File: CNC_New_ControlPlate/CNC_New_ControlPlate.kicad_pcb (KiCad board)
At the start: 2 copper layers, 1 part

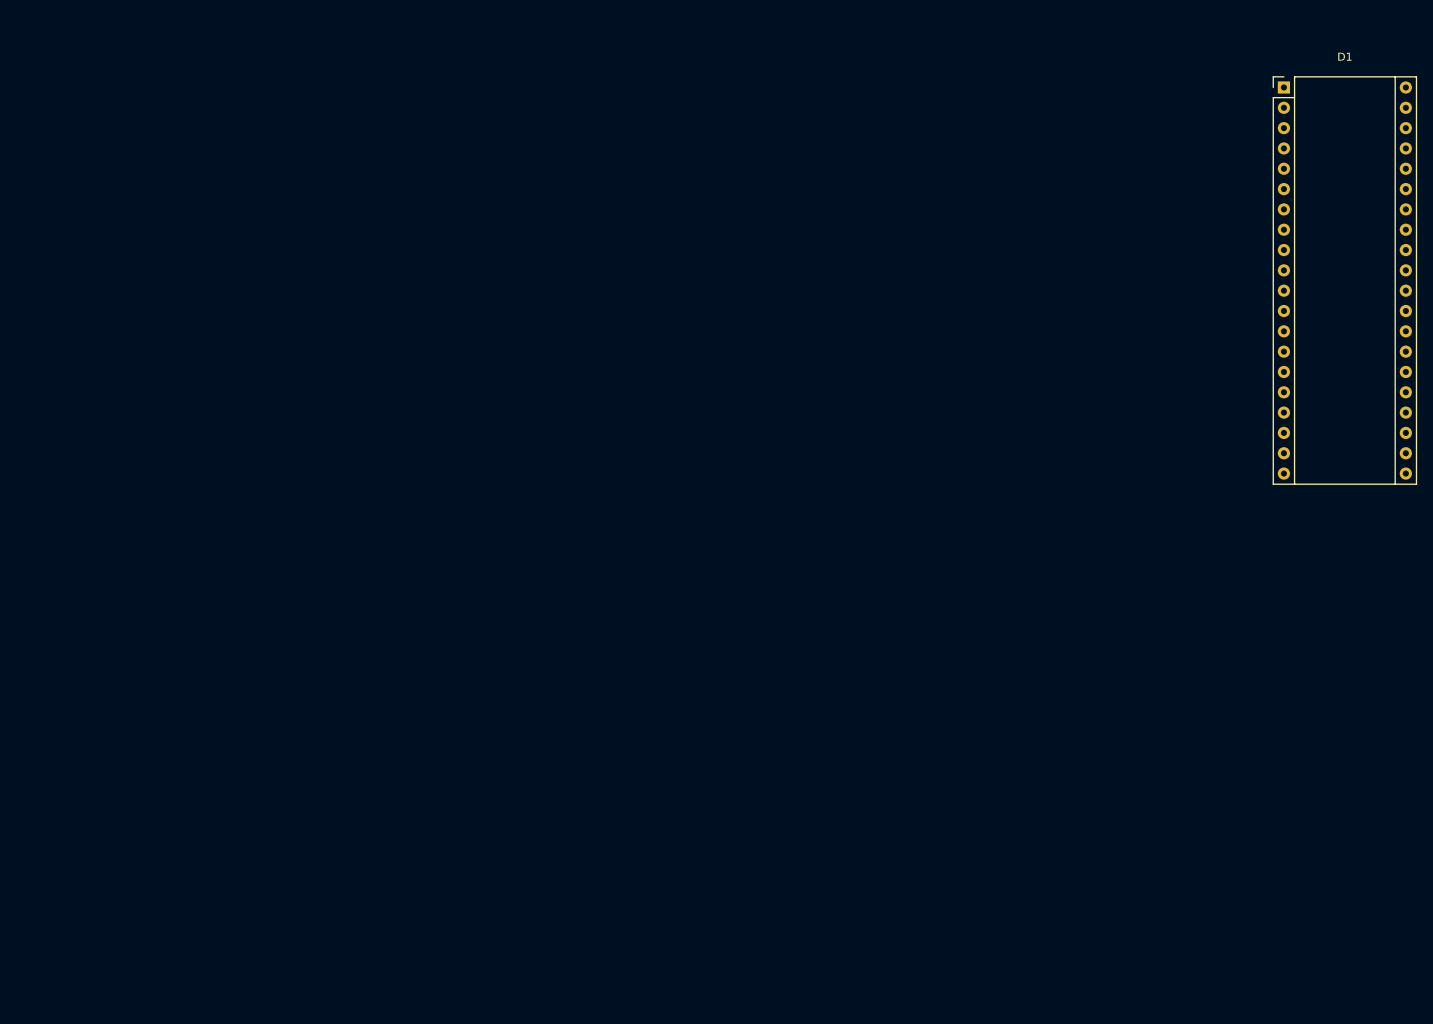
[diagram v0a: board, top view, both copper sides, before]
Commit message: [*] Порядок выводов на разъёме Others [*] Порядок выводов на разъёме Pause [*] Порядок подключения каналов на драйвере диф. линий [+] Начата расстановка pcb схемы
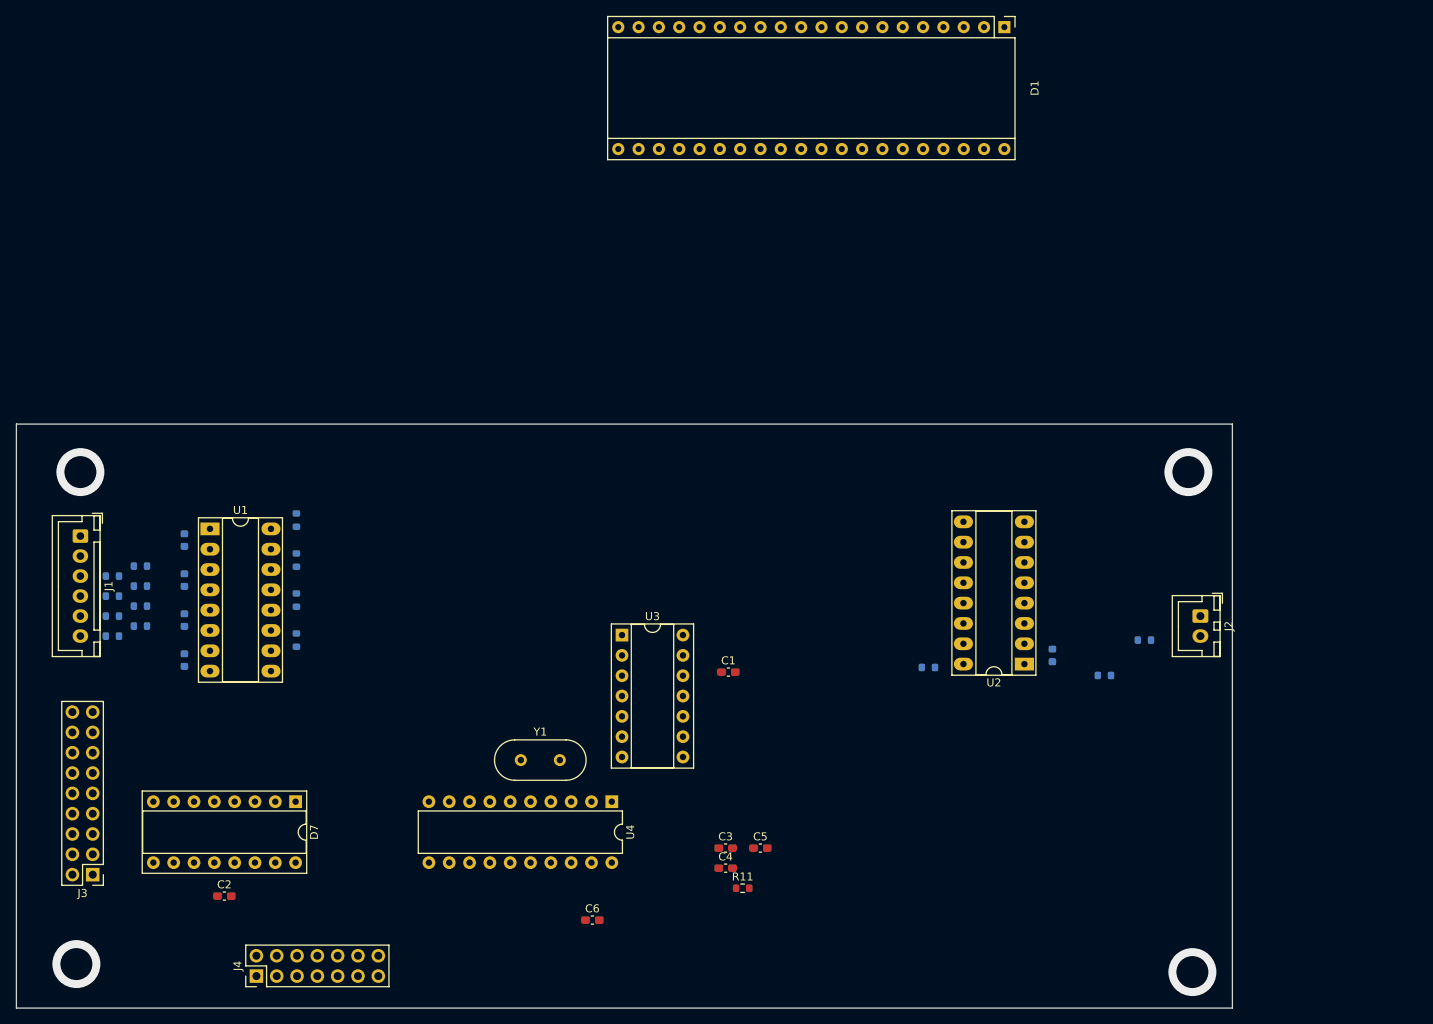
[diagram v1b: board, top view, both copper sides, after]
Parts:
- added C1: 100 nF, Capacitor_SMD:C_0603_1608Metric_Pad1.08x0.95mm_HandSolder, F.Cu at (149.0, 108.0)
- added C2: 100 nF, Capacitor_SMD:C_0603_1608Metric_Pad1.08x0.95mm_HandSolder, F.Cu at (86.0, 136.0)
- added C3: 100n, Capacitor_SMD:C_0603_1608Metric_Pad1.08x0.95mm_HandSolder, F.Cu at (148.7, 130.0)
- added C4: 22 pF, Capacitor_SMD:C_0603_1608Metric_Pad1.08x0.95mm_HandSolder, F.Cu at (148.7, 132.5)
- added C5: 22 pF, Capacitor_SMD:C_0603_1608Metric_Pad1.08x0.95mm_HandSolder, F.Cu at (153.0, 130.0)
- added C6: 100n, Capacitor_SMD:C_0603_1608Metric_Pad1.08x0.95mm_HandSolder, F.Cu at (132.0, 139.0)
- added D2: D_Zener_1.3V, Diode_SMD:D_0603_1608Metric, B.Cu at (189.5, 105.9)
- added D3: D_Zener_1.3V, Diode_SMD:D_0603_1608Metric, B.Cu at (81.0, 91.5)
- added D4: D_Zener_1.3V, Diode_SMD:D_0603_1608Metric, B.Cu at (81.0, 96.5)
- added D5: D_Zener_1.3V, Diode_SMD:D_0603_1608Metric, B.Cu at (81.0, 101.5)
- added D6: D_Zener_1.3V, Diode_SMD:D_0603_1608Metric, B.Cu at (81.0, 106.5)
- added D7: SN75ALS192N, Package_DIP:DIP-16_W7.62mm_Socket, F.Cu at (94.9, 124.2)
- added FB1: FerriteBead, Resistor_SMD:R_0603_1608Metric, B.Cu at (72.0, 96.0)
- added FB2: FerriteBead, Resistor_SMD:R_0603_1608Metric, B.Cu at (72.0, 98.5)
- added FB3: FerriteBead, Resistor_SMD:R_0603_1608Metric, B.Cu at (72.0, 101.0)
- added FB4: FerriteBead, Resistor_SMD:R_0603_1608Metric, B.Cu at (72.0, 103.5)
- added FB5: FerriteBead, Resistor_SMD:R_0603_1608Metric, B.Cu at (201.0, 104.0)
- added J1: OTHER, Connector_JST:JST_XH_B6B-XH-A_1x06_P2.50mm_Vertical, F.Cu at (68.0, 91.0)
- added J2: Conn_01x02, Connector_JST:JST_XH_B2B-XH-A_1x02_P2.50mm_Vertical, F.Cu at (208.0, 101.0)
- added J3: STEPPERS, Connector_PinHeader_2.54mm:PinHeader_2x09_P2.54mm_Vertical, F.Cu at (69.5, 133.3)
- added J4: SPINDEL, Connector_PinHeader_2.54mm:PinHeader_2x07_P2.54mm_Vertical, F.Cu at (90.0, 146.0)
- added R1: 200, Resistor_SMD:R_0603_1608Metric, B.Cu at (196.0, 108.4)
- added R10: 330, Resistor_SMD:R_0603_1608Metric, B.Cu at (95.0, 104.0)
- added R11: 10k, Resistor_SMD:R_0603_1608Metric, F.Cu at (150.8, 135.0)
- added R2: 330, Resistor_SMD:R_0603_1608Metric, B.Cu at (174.0, 107.4)
- added R3: 200, Resistor_SMD:R_0603_1608Metric, B.Cu at (75.5, 94.8)
- added R4: 200, Resistor_SMD:R_0603_1608Metric, B.Cu at (75.5, 97.2)
- added R5: 200, Resistor_SMD:R_0603_1608Metric, B.Cu at (75.5, 99.8)
- added R6: 200, Resistor_SMD:R_0603_1608Metric, B.Cu at (75.5, 102.2)
- added R7: 330, Resistor_SMD:R_0603_1608Metric, B.Cu at (95.0, 89.0)
- added R8: 330, Resistor_SMD:R_0603_1608Metric, B.Cu at (95.0, 94.0)
- added R9: 330, Resistor_SMD:R_0603_1608Metric, B.Cu at (95.0, 99.0)
- added U1: PC847, Package_DIP:DIP-16_W7.62mm_Socket_LongPads, F.Cu at (84.2, 90.1)
- added U2: PC847, Package_DIP:DIP-16_W7.62mm_Socket_LongPads, F.Cu at (186.0, 107.0)
- added U3: 7406, Package_DIP:DIP-14_W7.62mm_Socket, F.Cu at (135.7, 103.4)
- added U4: ATtiny2313V-10P, Package_DIP:DIP-20_W7.62mm, F.Cu at (134.4, 124.2)
- added Y1: 4MHz, Crystal:Crystal_HC49-4H_Vertical, F.Cu at (123.0, 119.0)
- D1: value BluePill -> Blue_Pill
- moved D1 35.8 mm to (183.5, 27.4), turned to -90 degrees
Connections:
- D1 pad 1: /X_Limit_5V -> Z_HOME_3.3V
- D1 pad 10: /Disable_Steppers -> Z_EN_3.3V
- D1 pad 16: unconnected-(D1-Pad16) -> PAUSE_3.3V
- D1 pad 17: unconnected-(D1-Pad17) -> SENSOR_3.3V
- D1 pad 18: unconnected-(D1-Pad18) -> +5V
- D1 pad 19: unconnected-(D1-Pad19) -> GNDREF
- D1 pad 2: /Y_Limit_5V -> Y_HOME_3.3V
- D1 pad 25: /X_step_3.3V -> ~{X_STEP_3.3V}
- D1 pad 26: /Y_step_3.3V -> Y_STEP_3.3V
- D1 pad 27: /Z_step_3.3V -> Z_STEP_3.3V
- D1 pad 29: /X_dir_3.3V -> X_DIR_3.3V
- D1 pad 3: /Z_Limit_5V -> X_HOME_3.3V
- D1 pad 30: /Y_dir_3.3V -> ~{Y_DIR_3.3V}
- D1 pad 31: /Z_dir_3.3V -> Z_DIR_3.3V
- D1 pad 33: /Spindel_Dir_3.3V -> Spin_Dir
- D1 pad 34: /Spindel_ENB_3.3V -> Spin_En
- D1 pad 38: /3.3V -> +3V3
- D1 pad 39: /GND -> GNDREF
- D1 pad 40: /GND -> GNDREF
- D1 pad 5: /Spindel_PWM_3.3V -> Spin_PWM
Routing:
- net (no net): vias 0 -> 4
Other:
- board outline added: 152 x 73 mm

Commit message: [*] Разводка платы в один слой (осталось 7 перемычек)
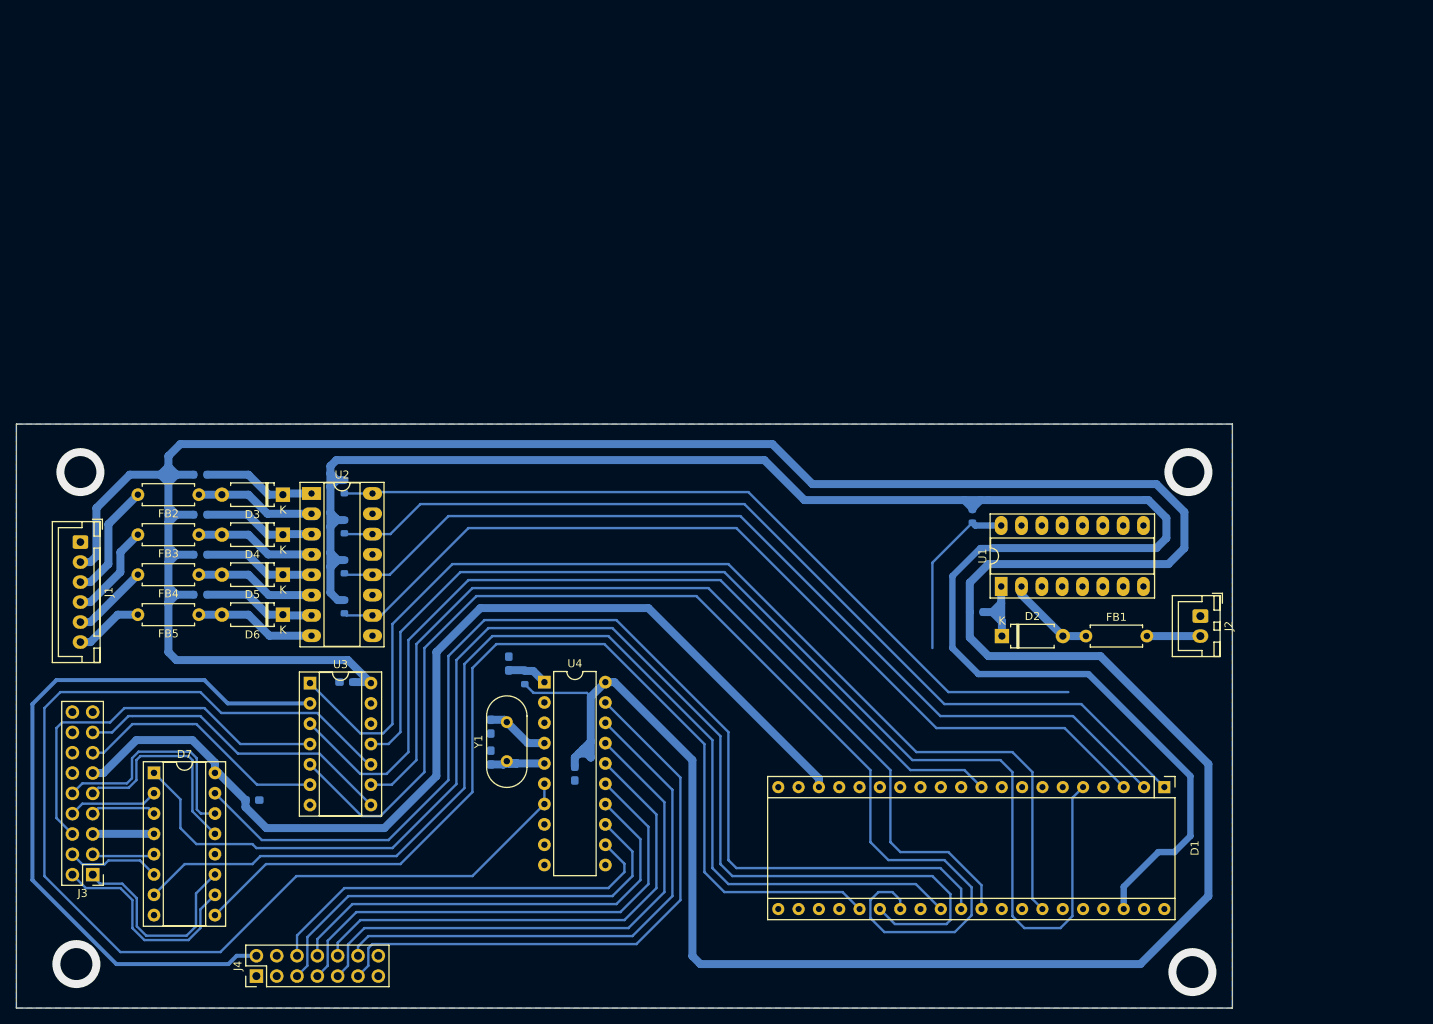
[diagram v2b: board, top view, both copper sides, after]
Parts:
- C1, C2, C3, C4, C5, C6, R11: moved to B.Cu
- D2, D3, D4, D5, D6: footprint Diode_SMD:D_0603_1608Metric -> Diode_THT:D_A-405_P7.62mm_Horizontal; moved to F.Cu
- FB1, FB2, FB3, FB4, FB5: footprint Resistor_SMD:R_0603_1608Metric -> Resistor_THT:R_Axial_DIN0207_L6.3mm_D2.5mm_P7.62mm_Horizontal; moved to F.Cu
- moved FB1 121.9 mm to (193.7, 103.5), turned to 0 degrees
- moved FB5 118.2 mm to (82.8, 100.8)
- moved U1 99.2 mm to (183.1, 97.3), turned to 90 degrees
- moved D1 97.1 mm to (203.5, 122.4)
- moved U2 91.6 mm to (96.9, 85.7), turned to 0 degrees
- moved C1 47.8 mm to (101.2, 109.2)
- moved U3 39.5 mm to (96.7, 109.4)
- moved R11 37.9 mm to (123.5, 108.7), turned to 90 degrees
- moved C5 37.0 mm to (119.3, 114.8), turned to 90 degrees
- moved C3 35.6 mm to (121.5, 106.9), turned to -90 degrees
- moved C4 32.4 mm to (119.3, 118.7), turned to -90 degrees
- moved R2 19.7 mm to (179.5, 88.5), turned to 90 degrees
- moved C6 18.4 mm to (129.8, 120.7), turned to 90 degrees
- moved D7 18.1 mm to (77.2, 120.6), turned to 0 degrees
- moved R1 17.9 mm to (180.0, 100.5), turned to 0 degrees
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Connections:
- D1 pad 26: Y_STEP_3.3V -> ~{Y_STEP_3.3V}
- D1 pad 29: X_DIR_3.3V -> ~{X_DIR_3.3V}
- D3 pad 1: Net-(U1-Pad1) -> Net-(R3-Pad2)
- D4 pad 1: Net-(U1-Pad3) -> Net-(R4-Pad2)
- D5 pad 1: Net-(U1-Pad5) -> Net-(D5-Pad1)
- D6 pad 1: Net-(U1-Pad7) -> Net-(R6-Pad2)
- D7 pad 1: ~{Y_DIR_3.3V} -> ~{Y_STEP_3.3V}
- D7 pad 10: X_DIR_p -> X_STEP_n
- D7 pad 11: X_DIR_n -> X_STEP_p
- D7 pad 13: X_STEP_p -> Y_DIR_p
- D7 pad 14: X_STEP_n -> Y_DIR_n
- D7 pad 15: ~{X_STEP_3.3V} -> ~{Y_DIR_3.3V}
- D7 pad 2: Y_DIR_n -> Y_STEP_n
- D7 pad 3: Y_DIR_p -> Y_STEP_p
- D7 pad 5: Y_STEP_n -> X_DIR_p
- D7 pad 6: Y_STEP_p -> X_DIR_n
- D7 pad 7: Y_STEP_3.3V -> ~{X_DIR_3.3V}
- D7 pad 9: X_DIR_3.3V -> ~{X_STEP_3.3V}
- FB1 pad 1: /HOME optocouplers/SENSOR_OP -> /HOME optocouplers/PAUSE_OP
- FB1 pad 2: SENSOR -> PAUSE
- FB2 pad 1: /HOME optocouplers/Z_HOME_OP -> /HOME optocouplers/SENSOR_OP
- FB2 pad 2: Z_HOME -> SENSOR
- FB3 pad 1: /HOME optocouplers/Y_HOME_OP -> /HOME optocouplers/Z_HOME_OP
- FB3 pad 2: Y_HOME -> Z_HOME
- FB4 pad 1: /HOME optocouplers/X_HOME_OP -> /HOME optocouplers/Y_HOME_OP
- FB4 pad 2: X_HOME -> Y_HOME
- FB5 pad 1: /HOME optocouplers/PAUSE_OP -> /HOME optocouplers/X_HOME_OP
- FB5 pad 2: PAUSE -> X_HOME
- R3 pad 2: Net-(U1-Pad1) -> Net-(R3-Pad2)
- R4 pad 2: Net-(U1-Pad3) -> Net-(R4-Pad2)
- R5 pad 2: Net-(U1-Pad5) -> Net-(D5-Pad1)
- R6 pad 2: Net-(U1-Pad7) -> Net-(R6-Pad2)
- U1 pad 1: Net-(U1-Pad1) -> Net-(D2-Pad1)
- U1 pad 10: X_HOME_3.3V -> unconnected-(U1-Pad10)
- U1 pad 11: GNDREF -> unconnected-(U1-Pad11)
- U1 pad 12: Y_HOME_3.3V -> unconnected-(U1-Pad12)
- U1 pad 13: GNDREF -> unconnected-(U1-Pad13)
- U1 pad 14: Z_HOME_3.3V -> unconnected-(U1-Pad14)
- U1 pad 16: SENSOR_3.3V -> PAUSE_3.3V
- U1 pad 2: /HOME optocouplers/SENSOR_OP -> /HOME optocouplers/PAUSE_OP
- U1 pad 3: Net-(U1-Pad3) -> unconnected-(U1-Pad3)
- U1 pad 4: /HOME optocouplers/Z_HOME_OP -> unconnected-(U1-Pad4)
- U1 pad 5: Net-(U1-Pad5) -> unconnected-(U1-Pad5)
- U1 pad 6: /HOME optocouplers/Y_HOME_OP -> unconnected-(U1-Pad6)
- U1 pad 7: Net-(U1-Pad7) -> unconnected-(U1-Pad7)
- U1 pad 8: /HOME optocouplers/X_HOME_OP -> unconnected-(U1-Pad8)
- U1 pad 9: GNDREF -> unconnected-(U1-Pad9)
- U2 pad 1: Net-(D2-Pad1) -> Net-(R3-Pad2)
- U2 pad 10: unconnected-(U2-Pad10) -> X_HOME_3.3V
- U2 pad 11: unconnected-(U2-Pad11) -> GNDREF
- U2 pad 12: unconnected-(U2-Pad12) -> Y_HOME_3.3V
- U2 pad 13: unconnected-(U2-Pad13) -> GNDREF
- U2 pad 14: unconnected-(U2-Pad14) -> Z_HOME_3.3V
- U2 pad 16: PAUSE_3.3V -> SENSOR_3.3V
- U2 pad 2: /HOME optocouplers/PAUSE_OP -> /HOME optocouplers/SENSOR_OP
- U2 pad 3: unconnected-(U2-Pad3) -> Net-(R4-Pad2)
- U2 pad 4: unconnected-(U2-Pad4) -> /HOME optocouplers/Z_HOME_OP
- U2 pad 5: unconnected-(U2-Pad5) -> Net-(D5-Pad1)
- U2 pad 6: unconnected-(U2-Pad6) -> /HOME optocouplers/Y_HOME_OP
- U2 pad 7: unconnected-(U2-Pad7) -> Net-(R6-Pad2)
- U2 pad 8: unconnected-(U2-Pad8) -> /HOME optocouplers/X_HOME_OP
- U2 pad 9: unconnected-(U2-Pad9) -> GNDREF
- U3 pad 1: Z_STEP_3.3V -> Spin_En
- U3 pad 10: unconnected-(U3-Pad10) -> Net-(U4-Pad6)
- U3 pad 11: Spin_Dir -> Spin_PWM
- U3 pad 12: SP_EN -> unconnected-(U3-Pad12)
- U3 pad 13: Spin_En -> unconnected-(U3-Pad13)
- U3 pad 2: Z_STEP -> SP_EN
- U3 pad 3: Z_DIR_3.3V -> Z_EN_3.3V
- U3 pad 4: Z_DIR -> Z_EN
- U3 pad 5: Z_EN_3.3V -> Z_STEP_3.3V
- U3 pad 6: Z_EN -> Z_STEP
- U3 pad 8: Net-(U3-Pad8) -> Z_DIR
- U3 pad 9: Spin_PWM -> Z_DIR_3.3V
- U4 pad 12: SP_8 -> SP_5
- U4 pad 13: SP_7 -> SP_1
- U4 pad 15: SP_5 -> SP_2
- U4 pad 16: SP_4 -> SP_7
- U4 pad 18: SP_2 -> SP_8
- U4 pad 19: SP_1 -> SP_4
- U4 pad 6: Net-(U3-Pad8) -> Net-(U4-Pad6)
- U4 pad 7: Net-(U3-Pad8) -> Net-(U4-Pad6)
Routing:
- net +5V: track 0.00 -> 590.4 mm
- net +3V3: track 0.00 -> 236.6 mm
- net ~{Y_STEP_3.3V}: track 0.00 -> 162.2 mm
- net Z_STEP_3.3V: track 0.00 -> 151.9 mm
- net Spin_PWM: track 0.00 -> 150.2 mm
- net ~{X_DIR_3.3V}: track 0.00 -> 144.3 mm
- net Net-(U4-Pad6): track 0.00 -> 143.0 mm
- net ~{Y_DIR_3.3V}: track 0.00 -> 142.0 mm
- net Spin_En: track 0.00 -> 137.4 mm
- net ~{X_STEP_3.3V}: track 0.00 -> 126.8 mm
- net Z_HOME_3.3V: track 0.00 -> 118.9 mm
- net Z_DIR_3.3V: track 0.00 -> 118.6 mm
- net Y_HOME_3.3V: track 0.00 -> 117.1 mm
- net Z_EN_3.3V: track 0.00 -> 115.5 mm
- net X_HOME_3.3V: track 0.00 -> 115.5 mm
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- added copper zone on B.Cu, net GNDREF

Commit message: [*] Разведена плата в один слой (3 перемычки на шине 5В; 2 соединения земли через плату STM
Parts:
- moved C1 4.32 mm to (100.5, 105.0), turned to -90 degrees
- moved R10 0.50 mm to (101.5, 99.8)
- moved R7 0.50 mm to (101.5, 84.8)
- moved R8 0.50 mm to (101.5, 89.8)
- moved R9 0.50 mm to (101.5, 94.8)
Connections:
- D3 pad 2: /HOME optocouplers/SENSOR_OP -> /HOME optocouplers/Z_HOME_OP
- D4 pad 2: /HOME optocouplers/Z_HOME_OP -> /HOME optocouplers/Y_HOME_OP
- D5 pad 2: /HOME optocouplers/Y_HOME_OP -> /HOME optocouplers/X_HOME_OP
- D6 pad 2: /HOME optocouplers/X_HOME_OP -> /HOME optocouplers/SENSOR_OP
- FB2 pad 1: /HOME optocouplers/SENSOR_OP -> /HOME optocouplers/Z_HOME_OP
- FB2 pad 2: SENSOR -> Z_HOME
- FB3 pad 1: /HOME optocouplers/Z_HOME_OP -> /HOME optocouplers/Y_HOME_OP
- FB3 pad 2: Z_HOME -> Y_HOME
- FB4 pad 1: /HOME optocouplers/Y_HOME_OP -> /HOME optocouplers/X_HOME_OP
- FB4 pad 2: Y_HOME -> X_HOME
- FB5 pad 1: /HOME optocouplers/X_HOME_OP -> /HOME optocouplers/SENSOR_OP
- FB5 pad 2: X_HOME -> SENSOR
- R10 pad 1: X_HOME_3.3V -> SENSOR_3.3V
- R7 pad 1: SENSOR_3.3V -> Z_HOME_3.3V
- R8 pad 1: Z_HOME_3.3V -> Y_HOME_3.3V
- R9 pad 1: Y_HOME_3.3V -> X_HOME_3.3V
- U2 pad 10: X_HOME_3.3V -> SENSOR_3.3V
- U2 pad 12: Y_HOME_3.3V -> X_HOME_3.3V
- U2 pad 14: Z_HOME_3.3V -> Y_HOME_3.3V
- U2 pad 16: SENSOR_3.3V -> Z_HOME_3.3V
- U2 pad 2: /HOME optocouplers/SENSOR_OP -> /HOME optocouplers/Z_HOME_OP
- U2 pad 4: /HOME optocouplers/Z_HOME_OP -> /HOME optocouplers/Y_HOME_OP
- U2 pad 6: /HOME optocouplers/Y_HOME_OP -> /HOME optocouplers/X_HOME_OP
- U2 pad 8: /HOME optocouplers/X_HOME_OP -> /HOME optocouplers/SENSOR_OP
- U3 pad 1: Spin_En -> Spin_PWM
- U3 pad 10: Net-(U4-Pad6) -> unconnected-(U3-Pad10)
- U3 pad 11: Spin_PWM -> unconnected-(U3-Pad11)
- U3 pad 12: unconnected-(U3-Pad12) -> SP_EN
- U3 pad 13: unconnected-(U3-Pad13) -> Spin_En
- U3 pad 2: SP_EN -> Net-(U4-Pad6)
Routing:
- net PAUSE_3.3V: track 21.7 -> 129.1 mm
- net +5V: track 590.4 -> 655.5 mm
- net SENSOR_3.3V: track 100.9 -> 158.6 mm
- net GNDREF: track 0.54 -> 52.6 mm
- net +3V3: track 236.6 -> 187.1 mm
- net Spin_PWM: track 150.2 -> 163.6 mm
- net Spin_En: track 137.4 -> 124.0 mm
- net SP_EN: track 91.9 -> 103.8 mm
- net Net-(U4-Pad6): track 143.0 -> 132.3 mm
- net SENSOR: track 14.6 -> 23.5 mm
- net Z_HOME: track 12.1 -> 17.1 mm
- net Y_HOME: track 9.64 -> 14.6 mm
- net X_HOME: track 8.61 -> 12.1 mm
- net Y_HOME_3.3V: track 117.1 -> 114.5 mm
- net Z_DIR_3.3V: track 118.6 -> 120.3 mm
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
